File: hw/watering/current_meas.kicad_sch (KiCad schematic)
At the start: 7 parts, among them U8 MCP6002-xSN

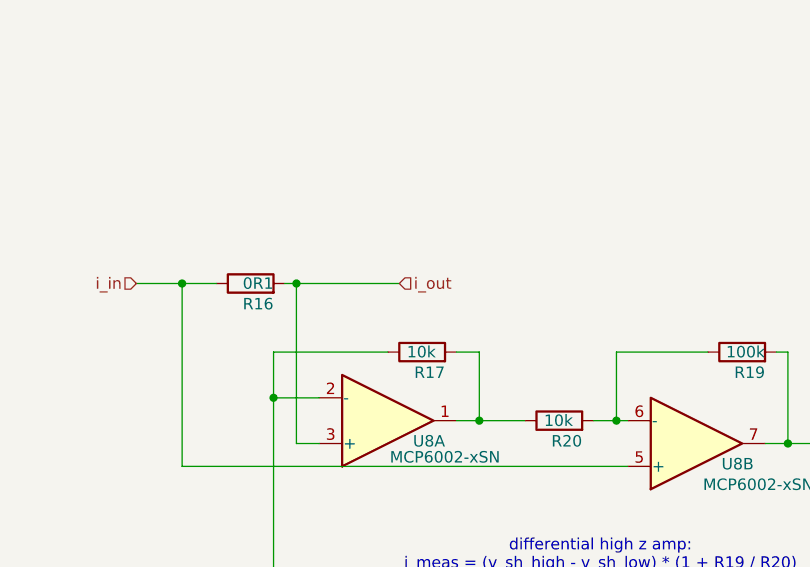
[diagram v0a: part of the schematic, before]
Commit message: reduced pcb size
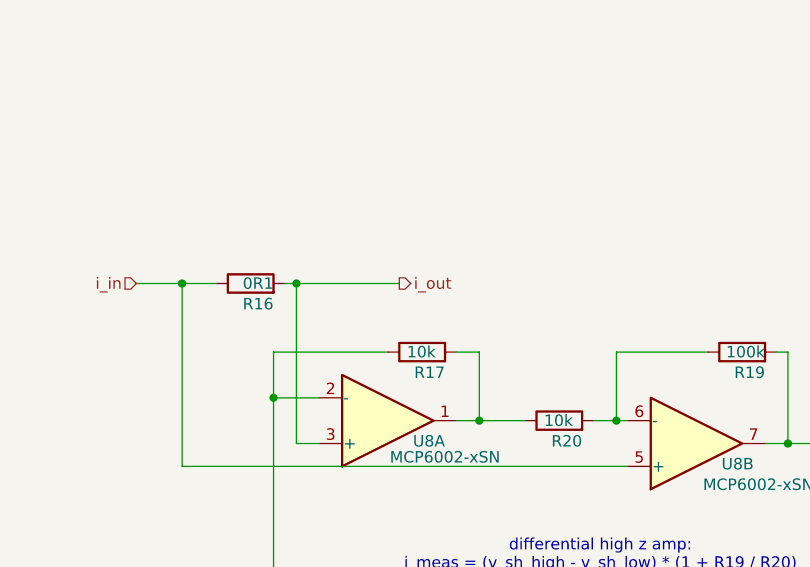
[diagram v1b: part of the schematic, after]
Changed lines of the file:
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@@
 	)
 	(hierarchical_label "i_out"
-		(shape input)
+		(shape output)
 		(at 113.03 91.44 0)
 		(effects
